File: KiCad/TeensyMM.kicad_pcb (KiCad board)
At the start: 4 copper layers, 22 x 22 mm, 14 parts, among them J1 MICROMOD-2222, U1 MK20DX256VLH7, U2 MKL02Z32VFG4, Y1 16MHz

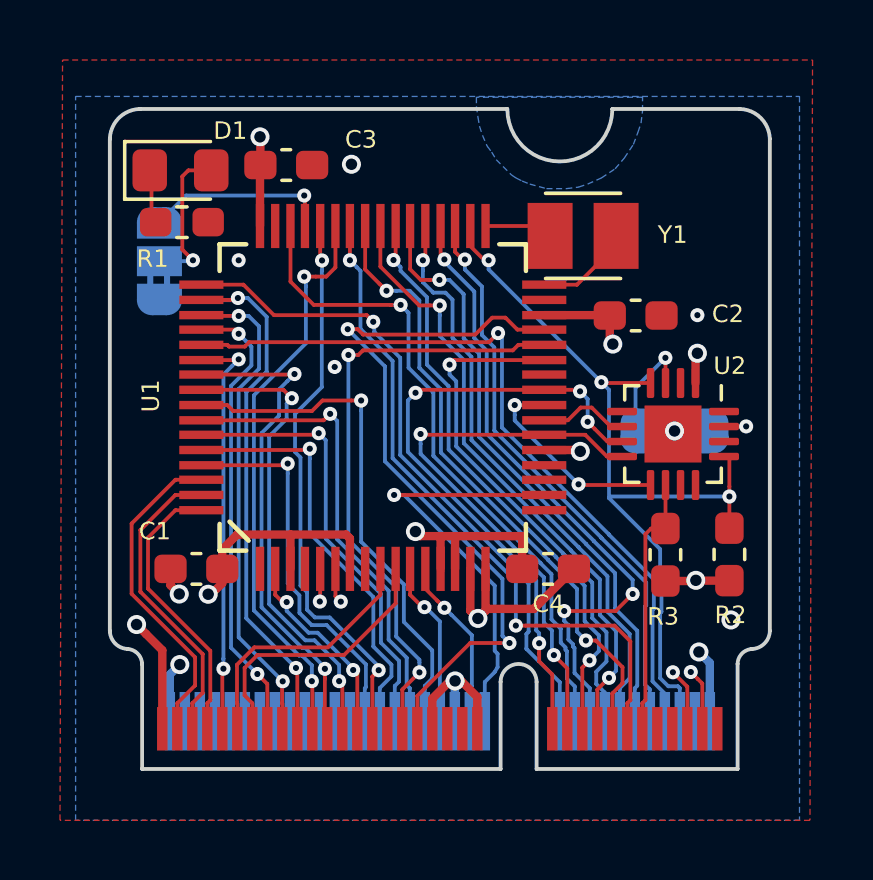
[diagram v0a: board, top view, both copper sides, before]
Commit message: Added RTC crystal, and v_bat circuitry. Needs cleanup
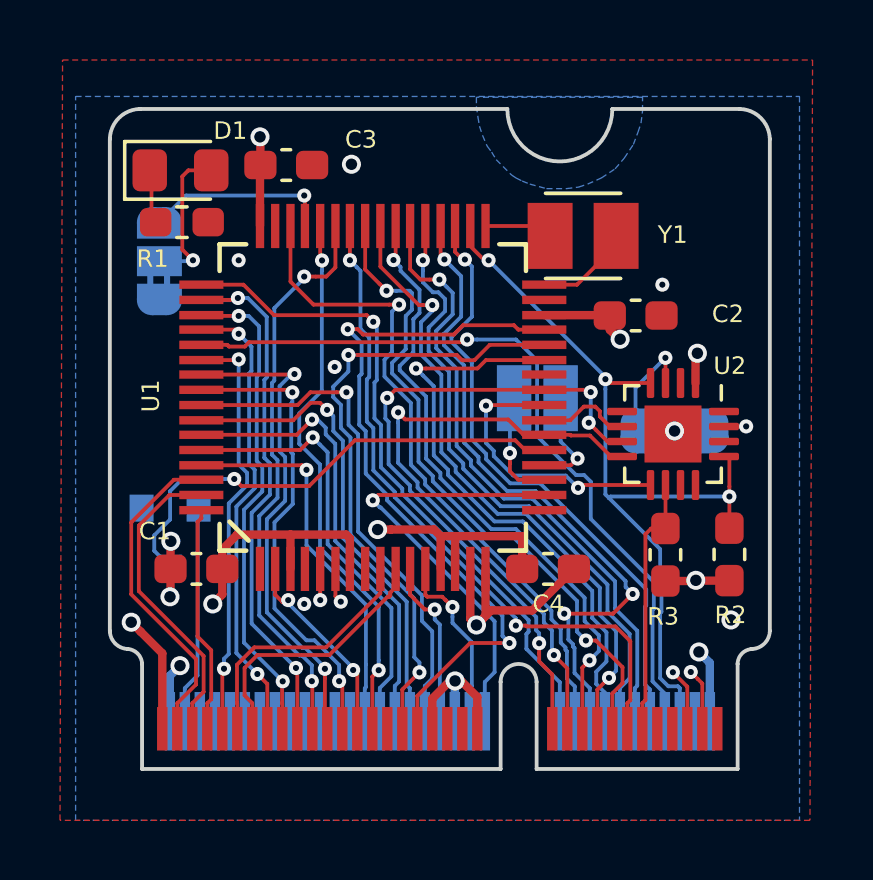
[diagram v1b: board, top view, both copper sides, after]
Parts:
- added D2: D_Schottky_x2_KCom_AAK, Package_TO_SOT_SMD:SOT-23, B.Cu at (123.2, 67.9)
- added Y2: 16MHz, footprints:OSC_XRCHA16M000F0A01R0, B.Cu at (135.4, 63.3)
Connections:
- J1 pad 72: (no net) -> RTC3V
- U1 pad 19: (no net) -> Net-(U1-Pad19)
- U1 pad 20: (no net) -> Net-(U1-Pad20)
- U1 pad 21: +3V3 -> Net-(D2-Pad3)
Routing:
- net Net-(D2-Pad3): track 0.00 -> 16.5 mm, vias 0 -> 1
- net RTC3V: track 0.00 -> 6.98 mm
- net Net-(U1-Pad19): track 0.00 -> 3.75 mm, vias 0 -> 1
- net Net-(U1-Pad20): track 0.00 -> 3.45 mm, vias 0 -> 1
- net /PTB1: track 6.92 -> 9.44 mm
- net SWD_CLK: track 19.1 -> 21.2 mm
- net D24-I2C-INT: track 17.5 -> 19.6 mm
- net D05-PTD7: track 9.43 -> 7.58 mm
- net GND: track 17.8 -> 19.4 mm, vias 9 -> 11
- net SWD_DIO: track 22.2 -> 23.5 mm
- net D16_A2: track 19.3 -> 20.4 mm
- net D32-CTS1: track 21.1 -> 22.1 mm
- net D00-RX1: track 19.9 -> 20.9 mm
- net D17_A3: track 21.5 -> 22.4 mm
- net D19-SCL0: track 19.8 -> 20.6 mm
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
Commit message: Cleanup board and gerbers
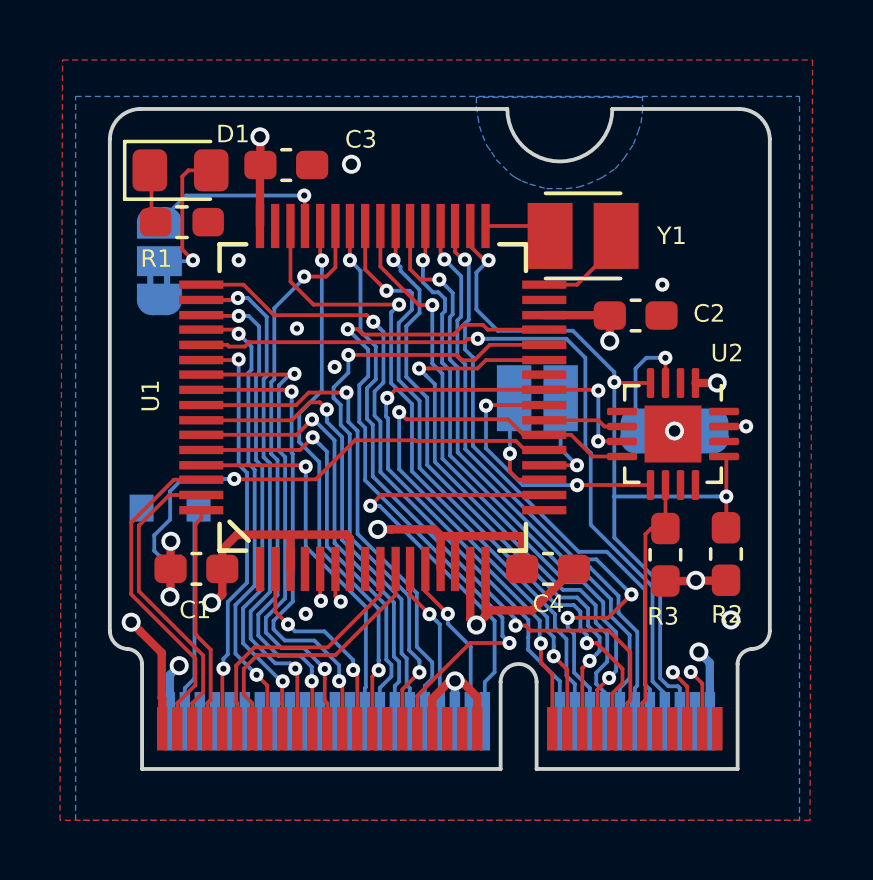
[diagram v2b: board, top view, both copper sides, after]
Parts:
- moved R2 0.12 mm to (141.7, 68.5)
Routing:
- net RESET: track 28.1 -> 29.0 mm
- net D28_A17: track 26.3 -> 27.2 mm
- net D17_A3: track 22.4 -> 21.6 mm
- net D19-SCL0: track 20.6 -> 20.1 mm
- net D18-SDA0: track 21.1 -> 20.5 mm
- net D16_A2: track 20.4 -> 19.9 mm
- net D01-TX1: track 21.4 -> 20.9 mm
- net +3V3: track 30.8 -> 30.4 mm, vias 9 -> 10
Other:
- board text added: "PTA1"
- board text added: "SWD debug"
- board text added: "lunOptics MicroMod_32 2020-12 V2.0"
- board text removed: "DE"
- board text removed: "PTA6"
- board text removed: "lunOptics MicroMod_32 2020-12 V1.0"

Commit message: Added Series Resistors on USB lines
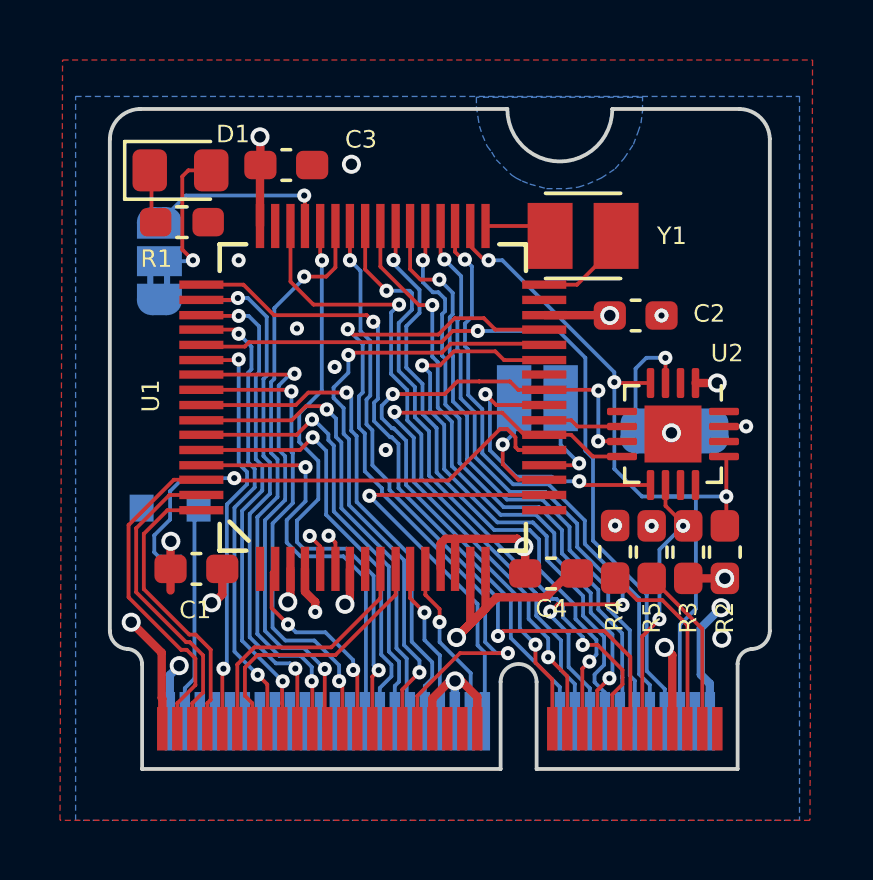
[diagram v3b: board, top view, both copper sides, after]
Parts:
- added R4: 33R, Resistor_SMD:R_0603_1608Metric_Pad1.05x0.95mm_HandSolder, F.Cu at (138.0, 68.4)
- added R5: 33R, Resistor_SMD:R_0603_1608Metric_Pad1.05x0.95mm_HandSolder, F.Cu at (139.2, 68.4)
- moved R3 0.77 mm to (140.4, 68.4)
- moved C4 0.18 mm to (135.9, 69.1)
- moved R2 0.07 mm to (141.7, 68.4)
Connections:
- J1 pad 3: USB-D+ -> Net-(J1-Pad3)
- J1 pad 5: USB-D- -> Net-(J1-Pad5)
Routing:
- net +3V3: track 30.4 -> 23.0 mm, vias 10 -> 12
- net Net-(J1-Pad5): track 0.00 -> 6.65 mm
- net GND: track 19.4 -> 25.6 mm, vias 11 -> 12
- net Net-(J1-Pad3): track 0.00 -> 5.71 mm
- net USB-D-: track 15.8 -> 10.9 mm
- net USB-D+: track 17.0 -> 13.1 mm
- net D05-PTD7: track 7.62 -> 9.83 mm
- net RESET: track 29.0 -> 27.0 mm
- net D22-A8: track 18.3 -> 19.7 mm
- net D06-PTD4: track 12.8 -> 14.2 mm
- net D17_A3: track 21.6 -> 22.6 mm
- net Net-(D2-Pad3): track 16.3 -> 16.9 mm
- net /PTB1: track 9.37 -> 9.88 mm
- net BOOT: track 8.72 -> 8.93 mm, vias 0 -> 2
